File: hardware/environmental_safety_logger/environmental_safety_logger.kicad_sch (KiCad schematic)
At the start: 11 parts, among them J1 Conn_01x07, J2 Conn_01x04, J3 Conn_01x07, J4 Conn_01x04, K1 G5Q-1, SW1 SMD_12x12mm_h8.5mm, U1 MQ-6

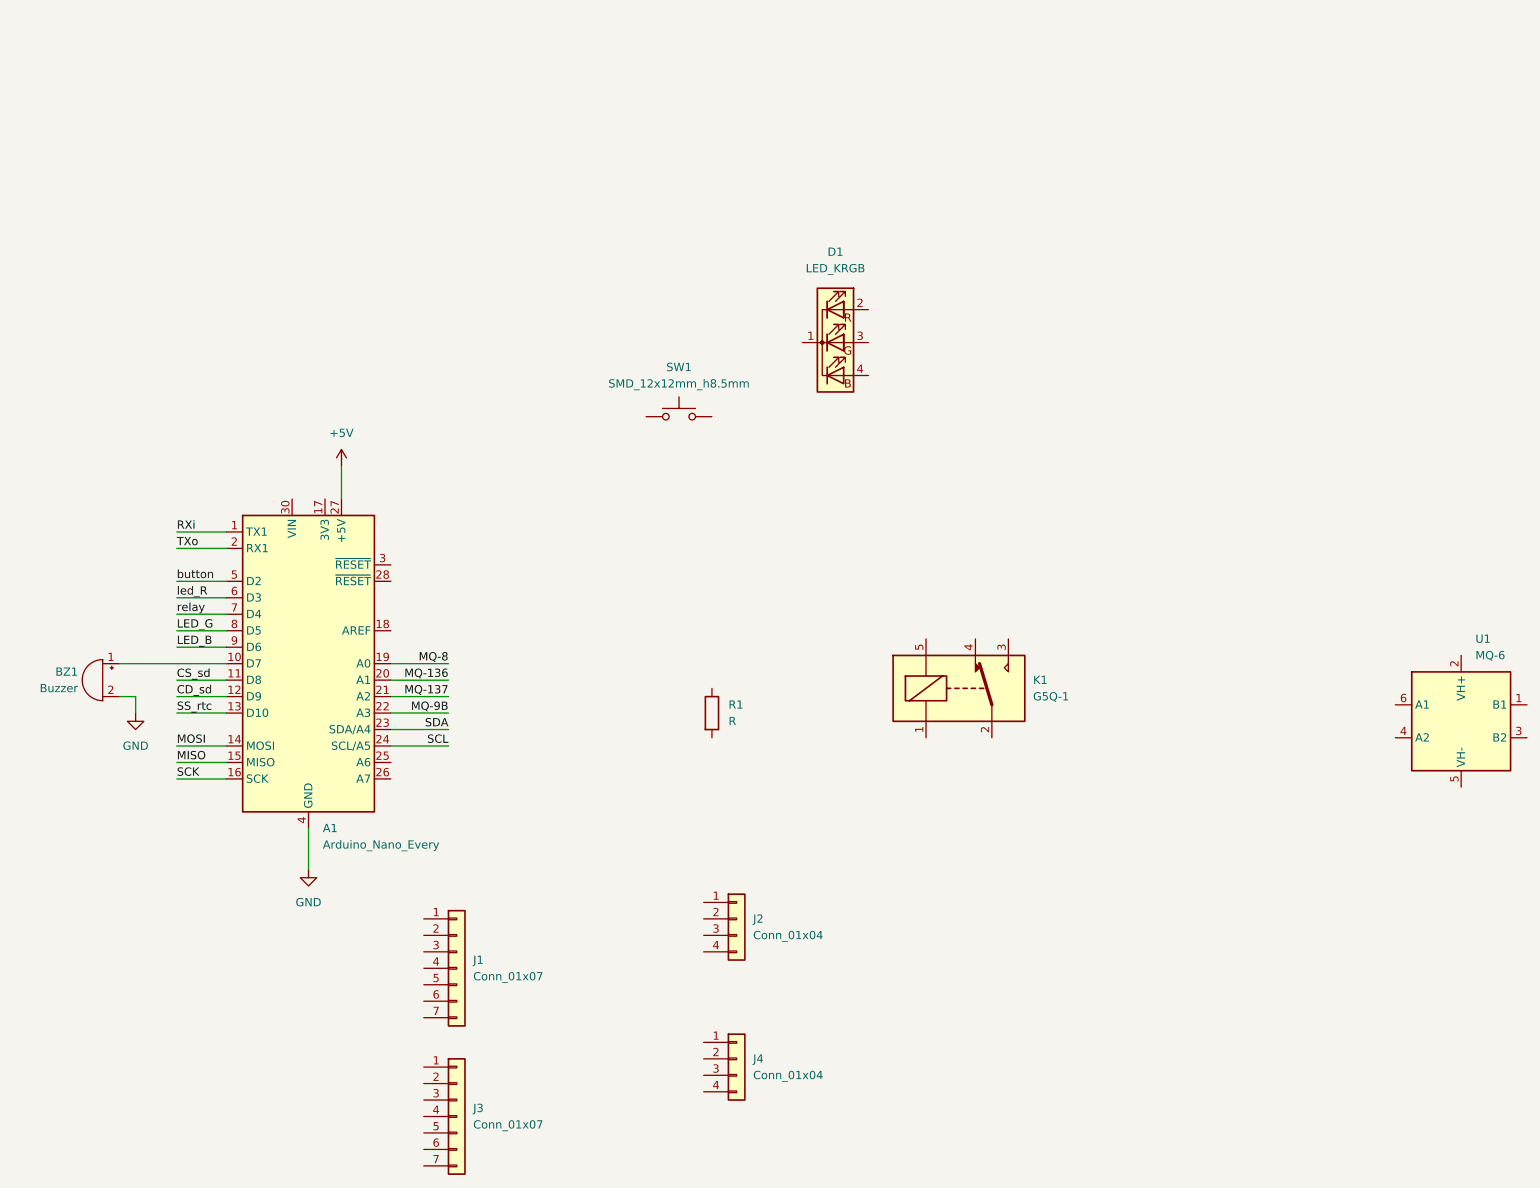
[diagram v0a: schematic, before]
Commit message: finished schematic and implemented
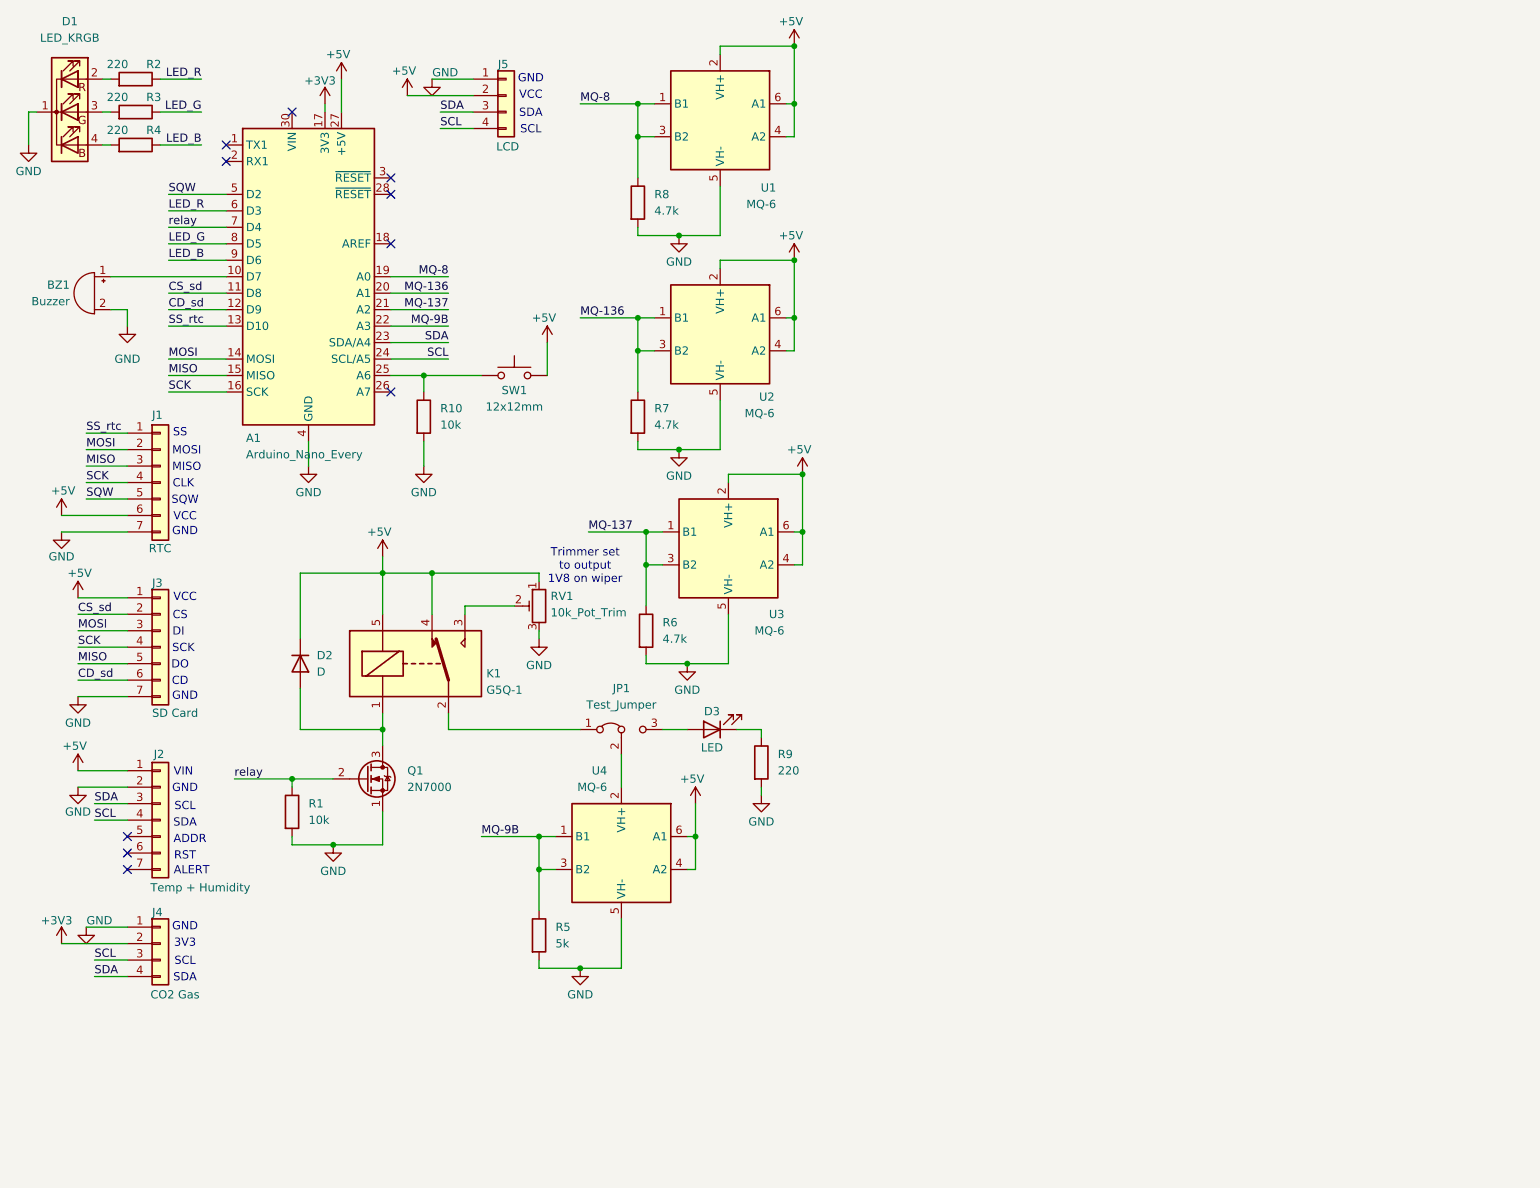
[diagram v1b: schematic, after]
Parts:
- removed J2: Conn_01x04, symbol Connector_Generic:Conn_01x04
- added D2: D, symbol Device:D
- added D3: LED, symbol Device:LED
- added J2: Temp + Humidity, symbol Connector_Generic:Conn_01x07
- added J5: LCD, symbol Connector_Generic:Conn_01x04
- added JP1: Test_Jumper, symbol Jumper:Jumper_3_Bridged12
- added Q1: 2N7000, Package_TO_SOT_THT:TO-92_Inline, symbol Transistor_FET:2N7000
- added R10: 10k, symbol Device:R
- added R2, R3, R4, R9: 220, symbol Device:R
- added R5: 5k, symbol Device:R
- added R6, R7, R8: 4.7k, symbol Device:R
- added RV1: 10k_Pot_Trim, symbol Device:R_Potentiometer_Trim
- added U2, U3, U4: MQ-6, Sensor:MQ-6, symbol Sensor_Gas:MQ-6
- J1: value Conn_01x07 -> RTC
- J3: value Conn_01x07 -> SD Card
- J4: value Conn_01x04 -> CO2 Gas
- R1: value R -> 10k
- SW1: value SMD_12x12mm_h8.5mm -> 12x12mm
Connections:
- net button is gone; now on net SQW: A1.5 (D2)
- net +5V: now also J1.6 (Pin_6), J3.1 (Pin_1), K1.4, K1.5, SW1.2, U1.2 (VH+), U1.4 (A2), U1.6 (A1), D2.1 (K), J2.1 (Pin_1), J5.2 (Pin_2), RV1.1, U2.2 (VH+), U2.4 (A2), U2.6 (A1), U3.2 (VH+), U3.4 (A2), U3.6 (A1), U4.4 (A2), U4.6 (A1)
- net CD_sd: now also J3.6 (Pin_6)
- net CS_sd: now also J3.2 (Pin_2)
- net GND: now also D1.1 (K), J1.7 (Pin_7), J3.7 (Pin_7), J4.1 (Pin_1), R1.2, U1.5 (VH-), J2.2 (Pin_2), J5.1 (Pin_1), Q1.1 (S), R10.2, R5.2, R6.2, R7.2, R8.2, R9.2, RV1.3, U2.5 (VH-), U3.5 (VH-), U4.5 (VH-)
- net LED_B: now also R4.1
- net LED_G: now also R3.1
- net MISO: now also J1.3 (Pin_3), J3.5 (Pin_5)
- net MOSI: now also J1.2 (Pin_2), J3.3 (Pin_3)
- net MQ-136: now also R7.1, U2.1 (B1), U2.3 (B2)
- net MQ-137: now also R6.1, U3.1 (B1), U3.3 (B2)
- net MQ-8: now also U1.1 (B1), U1.3 (B2), R8.1
- net MQ-9B: now also R5.1, U4.1 (B1), U4.3 (B2)
- net SCK: now also J1.4 (Pin_4), J3.4 (Pin_4)
- net SCL: now also J4.3 (Pin_3), J2.4 (Pin_4), J5.4 (Pin_4)
- net SDA: now also J4.4 (Pin_4), J2.3 (Pin_3), J5.3 (Pin_3)
- net SS_rtc: now also J1.1 (Pin_1)
- net relay: now also R1.1, Q1.2 (G)
- net at SW1.1: now also A1.25 (A6), R10.1
- net at K1.1: now also D2.2 (A), Q1.3 (D)
- net at K1.2: now also JP1.1 (A)
- net at K1.3: now also RV1.2
- net +3V3: now reaches J4.2 (Pin_2)
- net +3V3: now also A1.17 (3V3)
- net SQW: now reaches J1.5 (Pin_5)
- net at D1.2 (RA): now also R2.2
- net at D1.3 (GA): now also R3.2
- net at D1.4 (BA): now also R4.2
- net RXi: no longer names the net of A1.1 (TX1)
- net TXo: no longer names the net of A1.2 (RX1)
- net led_R renamed LED_R
- net LED_R: now also R2.1
- new net: JP1.2 (C), U4.2 (VH+)
- new net: D3.1 (K), R9.1
- new net: D3.2 (A), JP1.3 (B)
- no-connect marks 0 -> 10
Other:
- note added: "3V3"
- note added: "ADDR"
- note added: "ALERT"
- note added: "CD"
- note added: "CLK"
- note added: "CS"
- note added: "DI"
- note added: "DO"
- note added: "GND"
- note added: "MISO"
- note added: "MOSI"
- note added: "RST"
- note added: "SCK"
- note added: "SCL"
- note added: "SDA"
- note added: "SQW"
- note added: "SS"
- note added: "Trimmer set to output 1V8 on wiper"
- note added: "VCC"
- note added: "VIN"
- company: (none) -> FAST Research
- title: (none) -> Environmental Safety Logger
- moved on the sheet: A1, BZ1, D1, J1, J3, J4, K1, R1, SW1, U1
